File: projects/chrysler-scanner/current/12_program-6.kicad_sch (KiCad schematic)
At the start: 9 parts, among them Q12 HSW4602, Q8 HSW4602

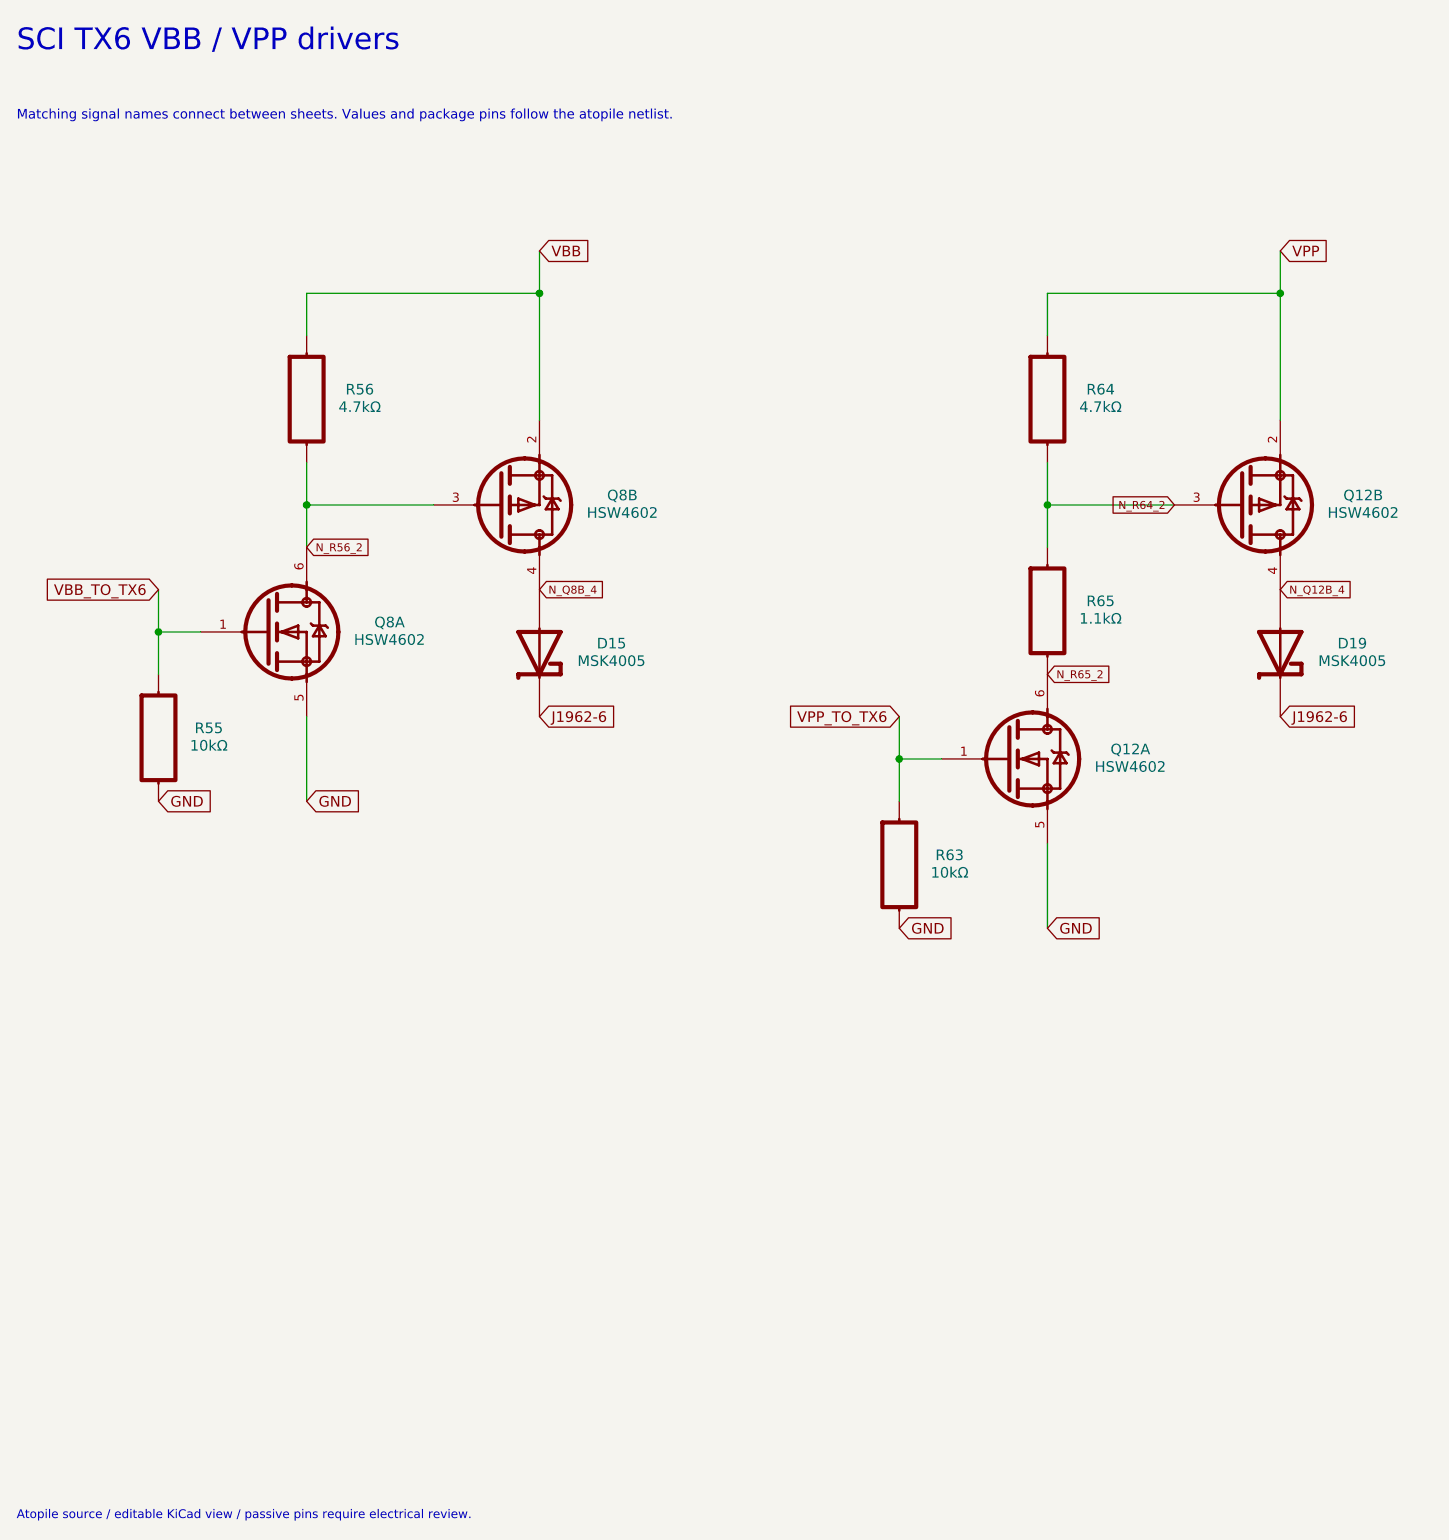
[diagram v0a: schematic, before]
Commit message: Finish scanner routing and add hierarchical system schematics
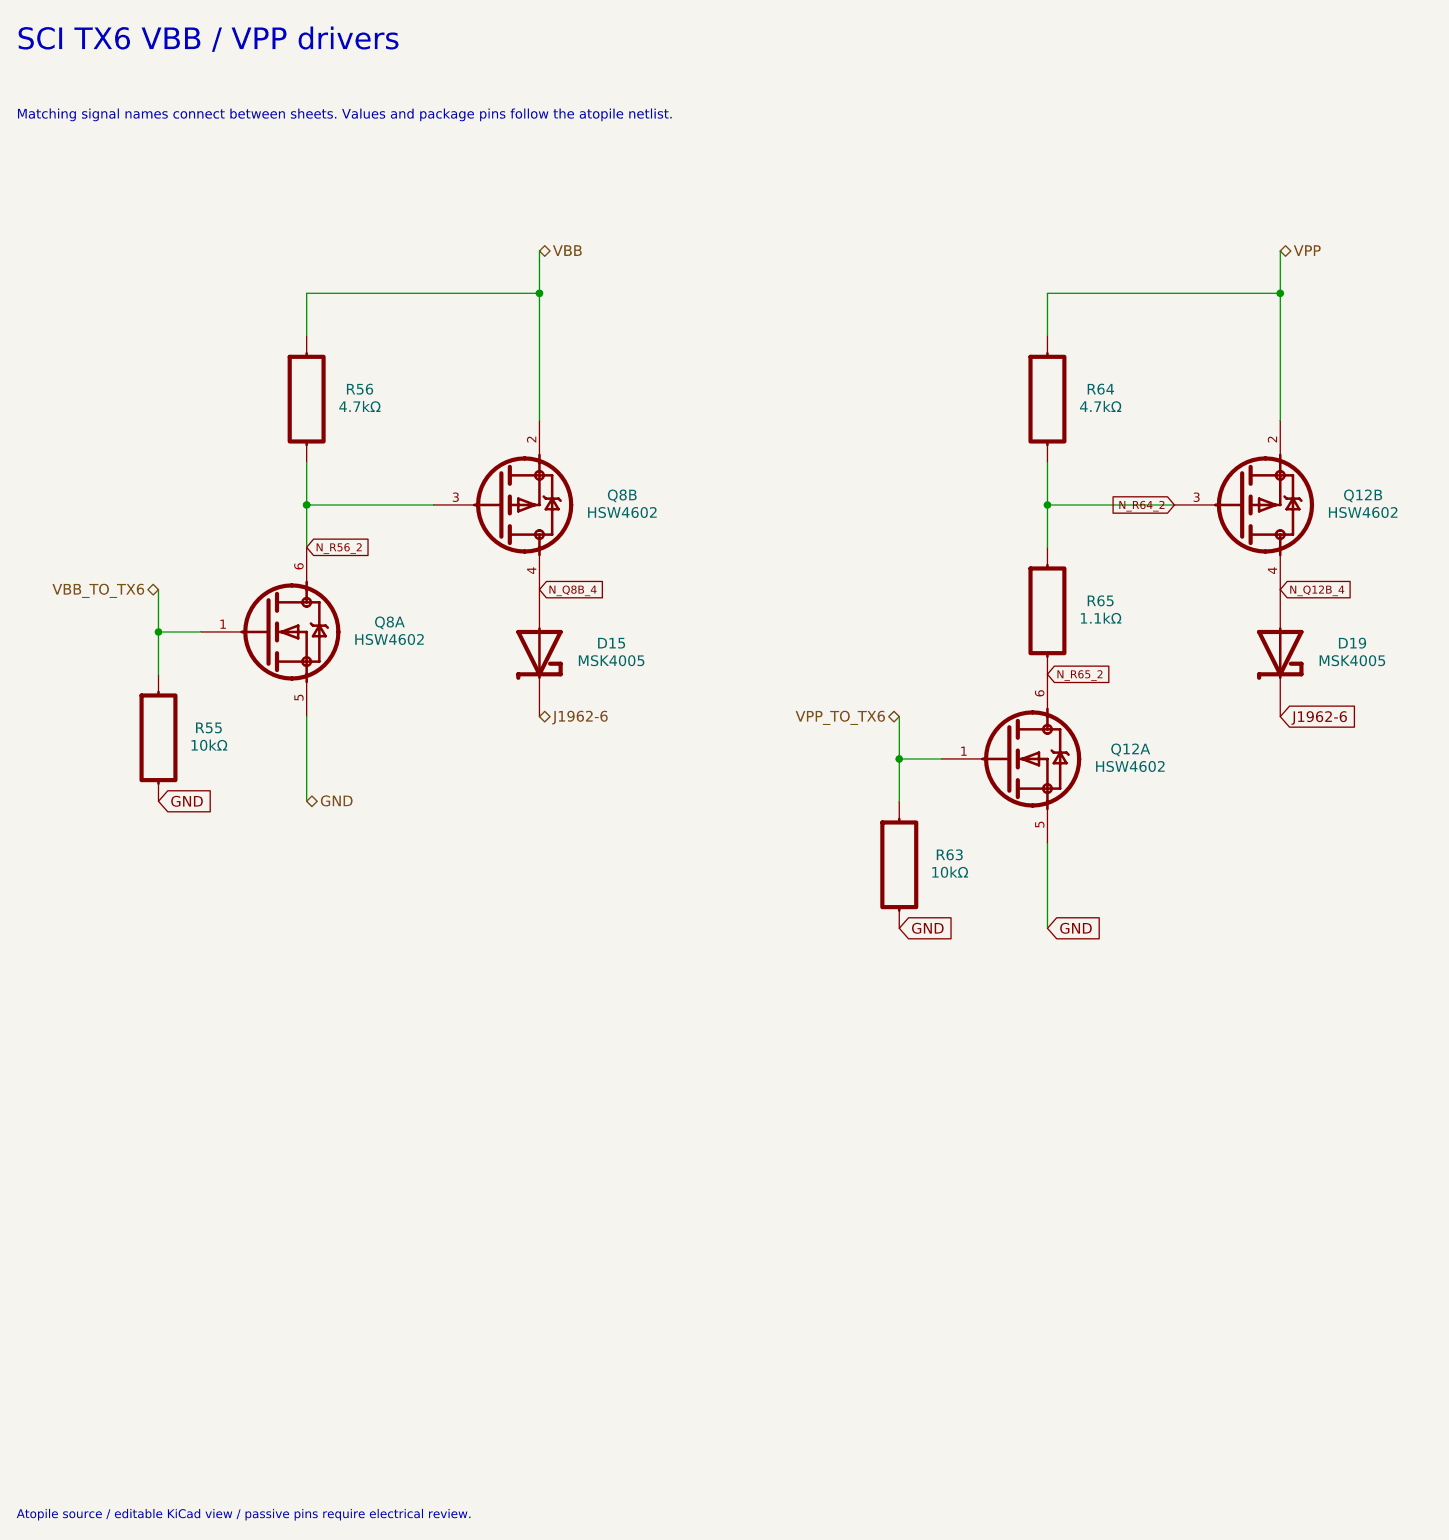
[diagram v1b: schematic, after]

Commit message: Fix scanner protection, ADC isolation and health watchdog
Coordinate the bounded 12 V input clamp and programming FET/capacitor ratings, add powered-off ADC isolation, and supervise the AW9523B permit with a dedicated GPIO13 health heartbeat. Preserve original placements and document all deliberate source-PDF deviations.

Validation: native ERC and full DRC/parity/refill report zero findings; strict preservation/connectivity audit and final adversarial review pass within the documented prototype bounds. Regenerate Rev C PDF, BOM, manufacturing exports, processing sites and verified portable archives. Compatible firmware and bench/mechanical qualification remain required.
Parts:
- Q12: value HSW4602 -> DMG6601LVT-7
- Q8: value HSW4602 -> DMC3071LVT-7
- R64: value 4.7kΩ -> 4.7k 1%
- R65: value 1.1kΩ -> 8.2k 1%

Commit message: Finish Chrysler scanner CCD correction and procurement fabrication package
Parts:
- D15, D19: value MSK4005 -> PMEG4005; Assembly (none) -> PLACE; MPN (none) -> PMEG4005EGWX; Manufacturer (none) -> Nexperia; Procurement Source (none) -> https://assets.nexperia.com/documents/data-sheet/PMEG4005EG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
- Q12: Assembly (none) -> PLACE; MPN (none) -> DMG6601LVT-7; Manufacturer (none) -> Diodes Incorporated; Procurement Source (none) -> https://www.diodes.com/datasheet/download/DMG6601LVT.pdf
- Q8: Assembly (none) -> PLACE; MPN (none) -> DMC3071LVT-7; Manufacturer (none) -> Diodes Incorporated; Procurement Source (none) -> https://www.diodes.com/datasheet/download/DMC3071LVT.pdf
- R55, R63: Assembly (none) -> PLACE; MPN (none) -> CRCW060310K0FKEA; Manufacturer (none) -> Vishay; Procurement Source (none) -> https://www.vishay.com/docs/20035/dcrcwe3.pdf; Selected Power Rating (none) -> 0.1W; Tolerance (none) -> 1%
- R56, R64: Assembly (none) -> PLACE; MPN (none) -> CRCW06034K70FKEA; Manufacturer (none) -> Vishay; Procurement Source (none) -> https://www.vishay.com/docs/20035/dcrcwe3.pdf; Selected Power Rating (none) -> 0.1W; Tolerance (none) -> 1%
- R65: Assembly (none) -> PLACE; MPN (none) -> CRCW06038K20FKEA; Manufacturer (none) -> Vishay; Procurement Source (none) -> https://www.vishay.com/docs/20035/dcrcwe3.pdf; Selected Power Rating (none) -> 0.1W; Tolerance (none) -> 1%
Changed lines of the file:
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@@
 			)
 		)
-		(property "Datasheet" ""
+		(property "Datasheet" "https://www.diodes.com/datasheet/download/DMG6601LVT.pdf"
 			(at 165.862 73.66 0)
 			(hide yes)
@@
 			)
 		)
-	)
+(property "Manufacturer" "Diodes Incorporated" (at 0 0 0) (effects (font (size 1 1)) (hide yes)))
+(property "MPN" "DMG6601LVT-7" (at 0 0 0) (effects (font (size 1 1)) (hide yes)))
+(property "Procurement Source" "https://www.diodes.com/datasheet/download/DMG6601LVT.pdf" (at 0 0 0) (effects (font (size 1 1)) (hide yes)))
+(property "Assembly" "PLACE" (at 0 0 0) (effects (font (size 1 1)) (hide yes)))
+)
 	(symbol
 		(lib_id "ChryslerScanner:R64")
@@
 			)
 		)
-		(property "Datasheet" ""
+		(property "Datasheet" "https://www.vishay.com/docs/20035/dcrcwe3.pdf"
 			(at 139.7 60.96 0)
 			(hide yes)
@@
 			)
 		)
-	)
+(property "Manufacturer" "Vishay" (at 0 0 0) (effects (font (size 1 1)) (hide yes)))
+(property "MPN" "CRCW06034K70FKEA" (at 0 0 0) (effects (font (size 1 1)) (hide yes)))
+(property "Procurement Source" "https://www.vishay.com/docs/20035/dcrcwe3.pdf" (at 0 0 0) (effects (font (size 1 1)) (hide yes)))
+(property "Assembly" "PLACE" (at 0 0 0) (effects (font (size 1 1)) (hide yes)))
+(property "Tolerance" "1%" (at 0 0 0) (effects (font (size 1 1)) (hide yes)))
+(property "Selected Power Rating" "0.1W" (at 0 0 0) (effects (font (size 1 1)) (hide yes)))
+)
 	(symbol
 		(lib_id "ChryslerScanner:R55")
@@
 			)
 		)
-		(property "Datasheet" ""
+		(property "Datasheet" "https://www.vishay.com/docs/20035/dcrcwe3.pdf"
 			(at 33.02 101.6 0)
 			(hide yes)
@@
 			)
 		)
-	)
+(property "Manufacturer" "Vishay" (at 0 0 0) (effects (font (size 1 1)) (hide yes)))
+(property "MPN" "CRCW060310K0FKEA" (at 0 0 0) (effects (font (size 1 1)) (hide yes)))
+(property "Procurement Source" "https://www.vishay.com/docs/20035/dcrcwe3.pdf" (at 0 0 0) (effects (font (size 1 1)) (hide yes)))
+(property "Assembly" "PLACE" (at 0 0 0) (effects (font (size 1 1)) (hide yes)))
+(property "Tolerance" "1%" (at 0 0 0) (effects (font (size 1 1)) (hide yes)))
+(property "Selected Power Rating" "0.1W" (at 0 0 0) (effects (font (size 1 1)) (hide yes)))
+)
 	(symbol
 		(lib_id "ChryslerScanner:Q12")
@@
 			)
 		)
-		(property "Datasheet" ""
+		(property "Datasheet" "https://www.diodes.com/datasheet/download/DMG6601LVT.pdf"
 			(at 137.922 104.14 0)
 			(hide yes)
@@
 			)
 		)
-	)
+(property "Manufacturer" "Diodes Incorporated" (at 0 0 0) (effects (font (size 1 1)) (hide yes)))
+(property "MPN" "DMG6601LVT-7" (at 0 0 0) (effects (font (size 1 1)) (hide yes)))
+(property "Procurement Source" "https://www.diodes.com/datasheet/download/DMG6601LVT.pdf" (at 0 0 0) (effects (font (size 1 1)) (hide yes)))
+(property "Assembly" "PLACE" (at 0 0 0) (effects (font (size 1 1)) (hide yes)))
+)
 	(symbol
 		(lib_id "power:GND")
@@
 			)
 		)
-		(property "Datasheet" ""
+		(property "Datasheet" "https://www.vishay.com/docs/20035/dcrcwe3.pdf"
 			(at 121.92 116.84 0)
 			(hide yes)
@@
 			)
 		)
-	)
+(property "Manufacturer" "Vishay" (at 0 0 0) (effects (font (size 1 1)) (hide yes)))
+(property "MPN" "CRCW060310K0FKEA" (at 0 0 0) (effects (font (size 1 1)) (hide yes)))
+(property "Procurement Source" "https://www.vishay.com/docs/20035/dcrcwe3.pdf" (at 0 0 0) (effects (font (size 1 1)) (hide yes)))
+(property "Assembly" "PLACE" (at 0 0 0) (effects (font (size 1 1)) (hide yes)))
+(property "Tolerance" "1%" (at 0 0 0) (effects (font (size 1 1)) (hide yes)))
+(property "Selected Power Rating" "0.1W" (at 0 0 0) (effects (font (size 1 1)) (hide yes)))
+)
 	(symbol
 		(lib_id "power:GND")
@@
 			)
 		)
-		(property "Datasheet" ""
+		(property "Datasheet" "https://www.vishay.com/docs/20035/dcrcwe3.pdf"
 			(at 50.8 60.96 0)
 			(hide yes)
@@
 			)
 		)
-	)
+(property "Manufacturer" "Vishay" (at 0 0 0) (effects (font (size 1 1)) (hide yes)))
+(property "MPN" "CRCW06034K70FKEA" (at 0 0 0) (effects (font (size 1 1)) (hide yes)))
+(property "Procurement Source" "https://www.vishay.com/docs/20035/dcrcwe3.pdf" (at 0 0 0) (effects (font (size 1 1)) (hide yes)))
+(property "Assembly" "PLACE" (at 0 0 0) (effects (font (size 1 1)) (hide yes)))
+(property "Tolerance" "1%" (at 0 0 0) (effects (font (size 1 1)) (hide yes)))
+(property "Selected Power Rating" "0.1W" (at 0 0 0) (effects (font (size 1 1)) (hide yes)))
+)
 	(symbol
 		(lib_id "ChryslerScanner:R65")
@@
 			)
 		)
-		(property "Datasheet" ""
+		(property "Datasheet" "https://www.vishay.com/docs/20035/dcrcwe3.pdf"
 			(at 139.7 86.36 0)
 			(hide yes)
@@
 			)
 		)
-	)
+(property "Manufacturer" "Vishay" (at 0 0 0) (effects (font (size 1 1)) (hide yes)))
+(property "MPN" "CRCW06038K20FKEA" (at 0 0 0) (effects (font (size 1 1)) (hide yes)))
+(property "Procurement Source" "https://www.vishay.com/docs/20035/dcrcwe3.pdf" (at 0 0 0) (effects (font (size 1 1)) (hide yes)))
+(property "Assembly" "PLACE" (at 0 0 0) (effects (font (size 1 1)) (hide yes)))
+(property "Tolerance" "1%" (at 0 0 0) (effects (font (size 1 1)) (hide yes)))
+(property "Selected Power Rating" "0.1W" (at 0 0 0) (effects (font (size 1 1)) (hide yes)))
+)
 	(symbol
 		(lib_id "power:GND")
@@
 			)
 		)
-		(property "Datasheet" ""
+		(property "Datasheet" "https://www.diodes.com/datasheet/download/DMC3071LVT.pdf"
 			(at 49.022 88.9 0)
 			(hide yes)
@@
 			)
 		)
-	)
+(property "Manufacturer" "Diodes Incorporated" (at 0 0 0) (effects (font (size 1 1)) (hide yes)))
+(property "MPN" "DMC3071LVT-7" (at 0 0 0) (effects (font (size 1 1)) (hide yes)))
+(property "Procurement Source" "https://www.diodes.com/datasheet/download/DMC3071LVT.pdf" (at 0 0 0) (effects (font (size 1 1)) (hide yes)))
+(property "Assembly" "PLACE" (at 0 0 0) (effects (font (size 1 1)) (hide yes)))
+)
 	(symbol
 		(lib_id "power:GND")
@@
 			)
 		)
-		(property "Value" "MSK4005"
+		(property "Value" "PMEG4005"
 			(at 87.3874 92.39 0)
 			(show_name no)
@@
 			)
 		)
-		(property "Datasheet" ""
+		(property "Datasheet" "https://assets.nexperia.com/documents/data-sheet/PMEG4005EGW.pdf"
 			(at 78.74 91.44 0)
 			(hide yes)
@@
 			)
 		)
-	)
+(property "Manufacturer" "Nexperia" (at 0 0 0) (effects (font (size 1 1)) (hide yes)))
+(property "MPN" "PMEG4005EGWX" (at 0 0 0) (effects (font (size 1 1)) (hide yes)))
+(property "Procurement Source" "https://assets.nexperia.com/documents/data-sheet/PMEG4005EGW.pdf" (at 0 0 0) (effects (font (size 1 1)) (hide yes)))
+(property "Assembly" "PLACE" (at 0 0 0) (effects (font (size 1 1)) (hide yes)))
+)
 	(symbol
 		(lib_id "ChryslerScanner:Q8")
@@
 			)
 		)
-		(property "Datasheet" ""
+		(property "Datasheet" "https://www.diodes.com/datasheet/download/DMC3071LVT.pdf"
 			(at 76.962 73.66 0)
 			(hide yes)
@@
 			)
 		)
-	)
+(property "Manufacturer" "Diodes Incorporated" (at 0 0 0) (effects (font (size 1 1)) (hide yes)))
+(property "MPN" "DMC3071LVT-7" (at 0 0 0) (effects (font (size 1 1)) (hide yes)))
+(property "Procurement Source" "https://www.diodes.com/datasheet/download/DMC3071LVT.pdf" (at 0 0 0) (effects (font (size 1 1)) (hide yes)))
+(property "Assembly" "PLACE" (at 0 0 0) (effects (font (size 1 1)) (hide yes)))
+)
 	(symbol
 		(lib_id "ChryslerScanner:D19")
@@
 			)
 		)
-		(property "Value" "MSK4005"
+		(property "Value" "PMEG4005"
 			(at 176.2874 92.39 0)
 			(show_name no)
@@
 			)
 		)
-		(property "Datasheet" ""
+		(property "Datasheet" "https://assets.nexperia.com/documents/data-sheet/PMEG4005EGW.pdf"
 			(at 167.64 91.44 0)
 			(hide yes)
@@
 			)
 		)
-	)
+(property "Manufacturer" "Nexperia" (at 0 0 0) (effects (font (size 1 1)) (hide yes)))
+(property "MPN" "PMEG4005EGWX" (at 0 0 0) (effects (font (size 1 1)) (hide yes)))
+(property "Procurement Source" "https://assets.nexperia.com/documents/data-sheet/PMEG4005EGW.pdf" (at 0 0 0) (effects (font (size 1 1)) (hide yes)))
+(property "Assembly" "PLACE" (at 0 0 0) (effects (font (size 1 1)) (hide yes)))
 )
+)
